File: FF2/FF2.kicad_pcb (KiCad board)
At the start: 2 copper layers, 154.8 x 140 mm, 76 parts, among them J1 AVR-ISP-6, SW1 RESET, SW2 BOOT, U1 ATmega328P-AU, Y1 16MHz

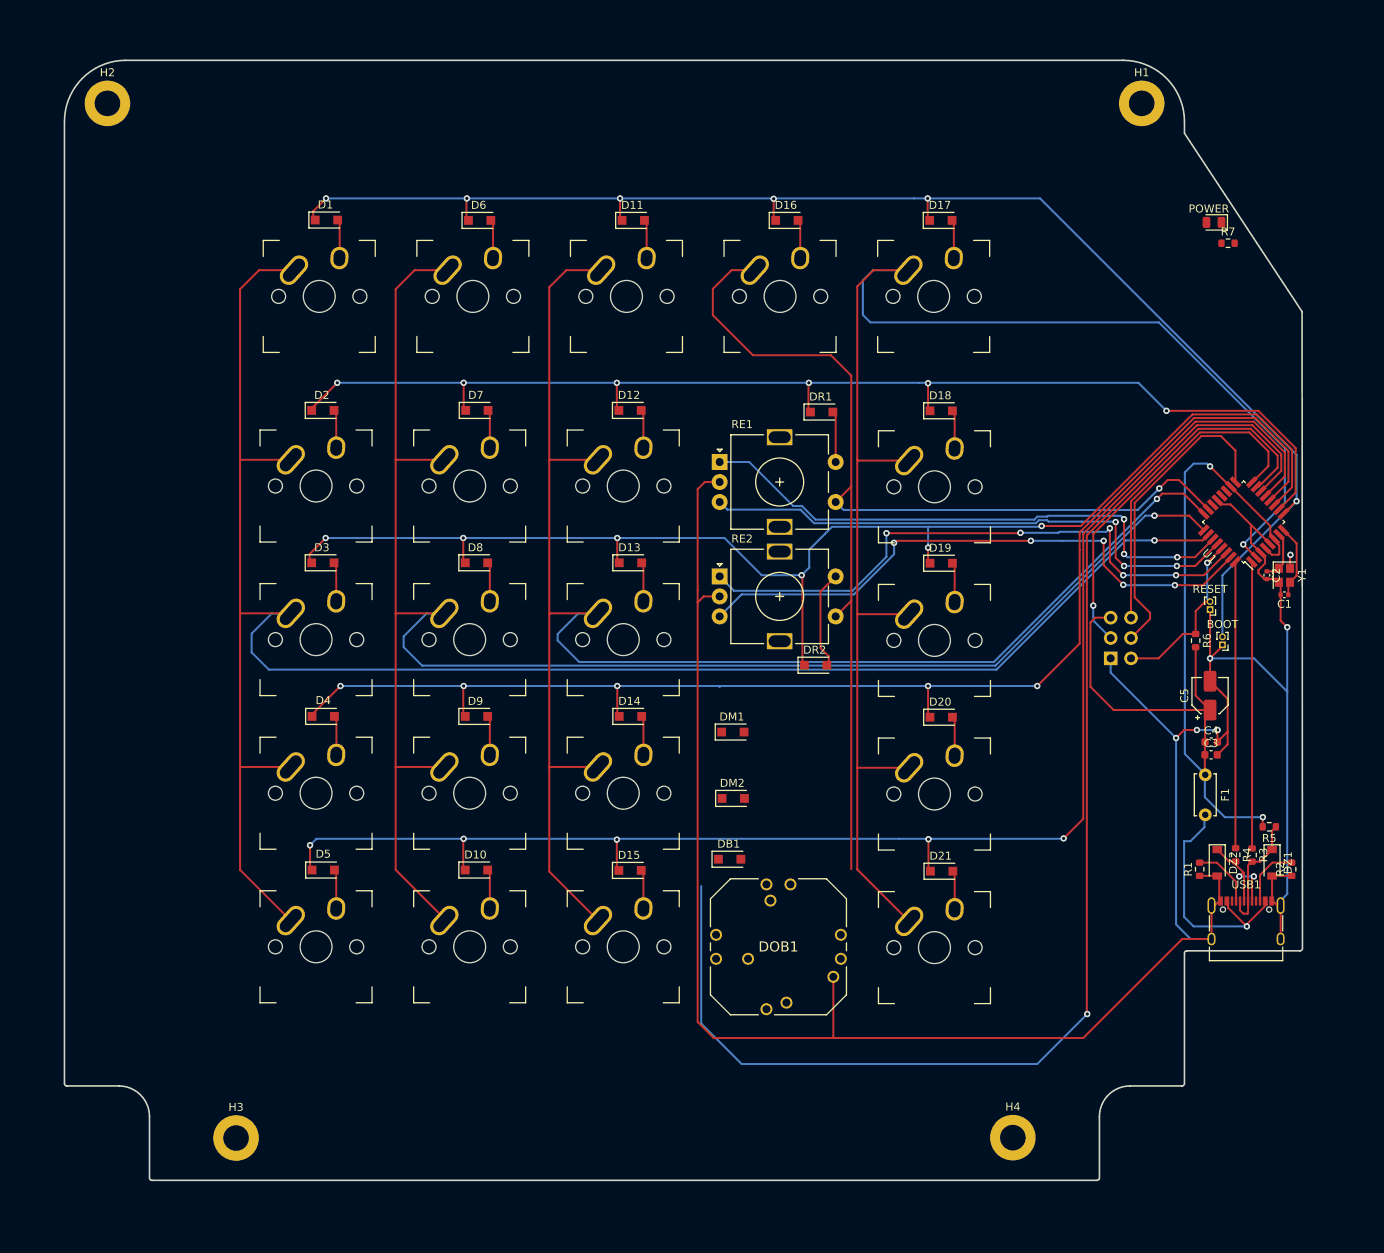
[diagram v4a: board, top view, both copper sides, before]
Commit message: updated silk values to be printed
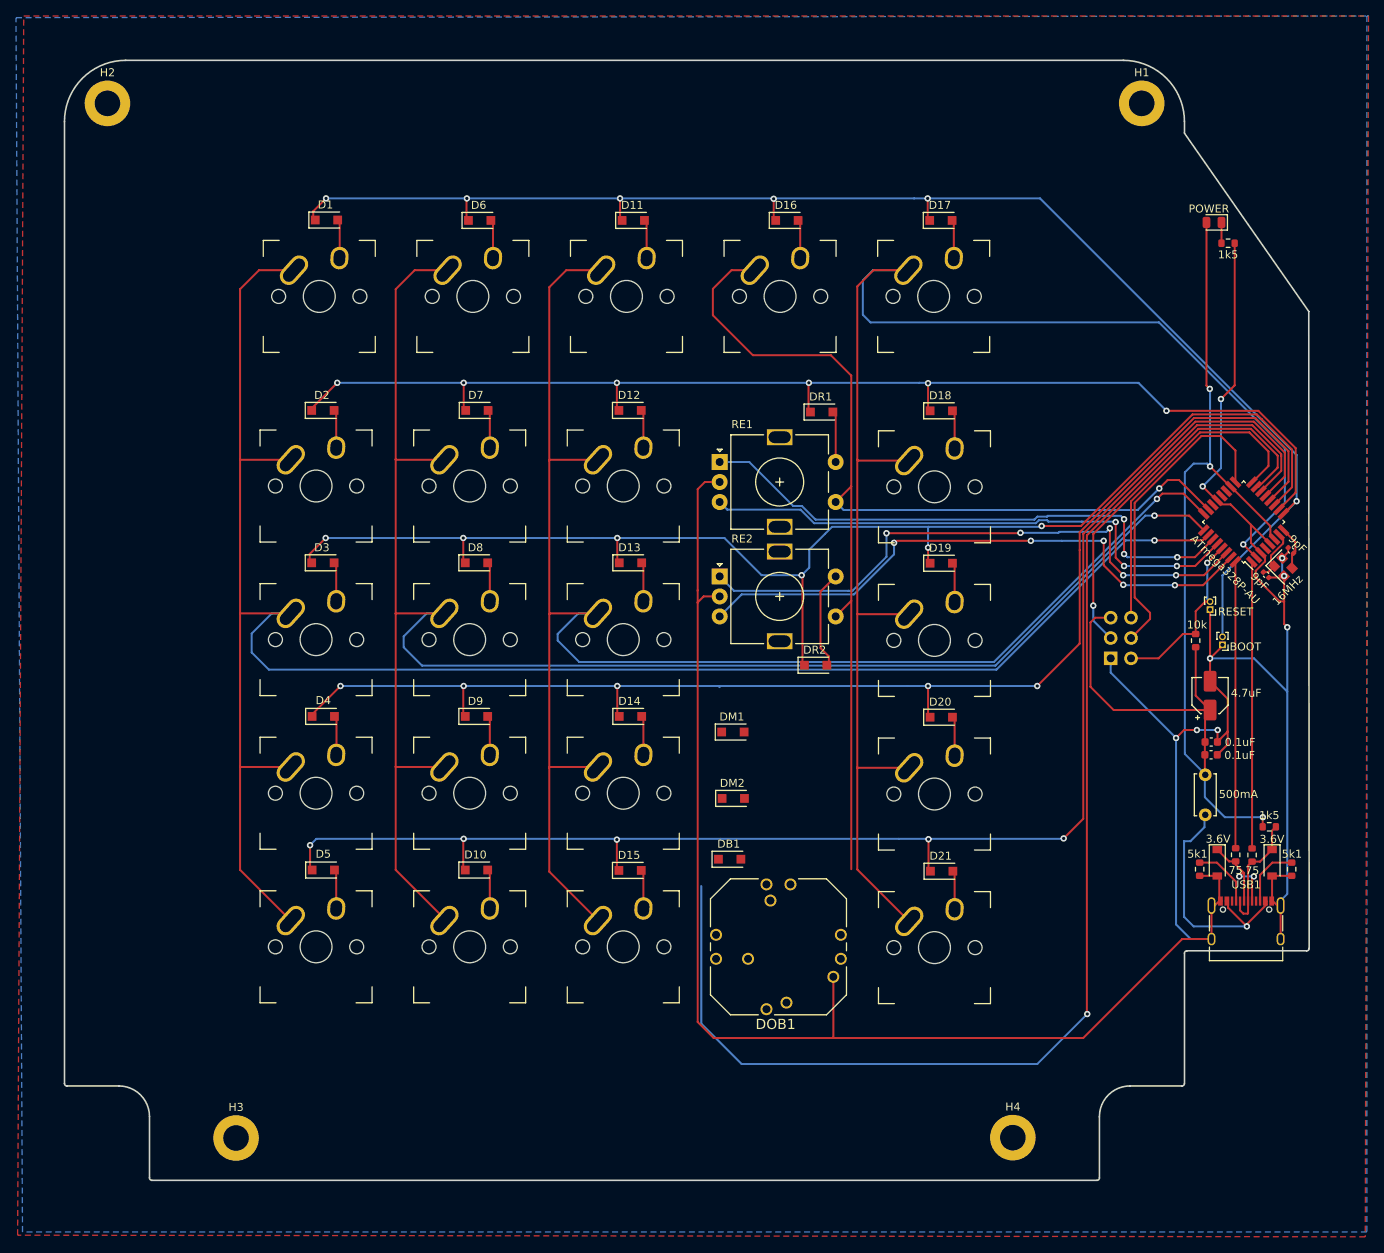
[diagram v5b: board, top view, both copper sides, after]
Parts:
- moved C1 5.61 mm to (235.1, 82.5), turned to 135 degrees
- moved Y1 1.03 mm to (234.1, 84.6), turned to 315 degrees
- moved C2 0.11 mm to (232.0, 85.6), turned to 315 degrees
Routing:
- net GND: track 319.3 -> 361.1 mm, vias 6 -> 9
- net +5V: track 115.4 -> 142.1 mm, vias 2 -> 3
- net CRYSTAL2: track 9.19 -> 5.51 mm
- net Net-(LED1-Pad1): track 0.00 -> 2.60 mm
- added copper zone on B.Cu, net GND
- added copper zone on F.Cu, net GND
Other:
- board size 154.8 x 140 mm -> 155.6 x 140 mm

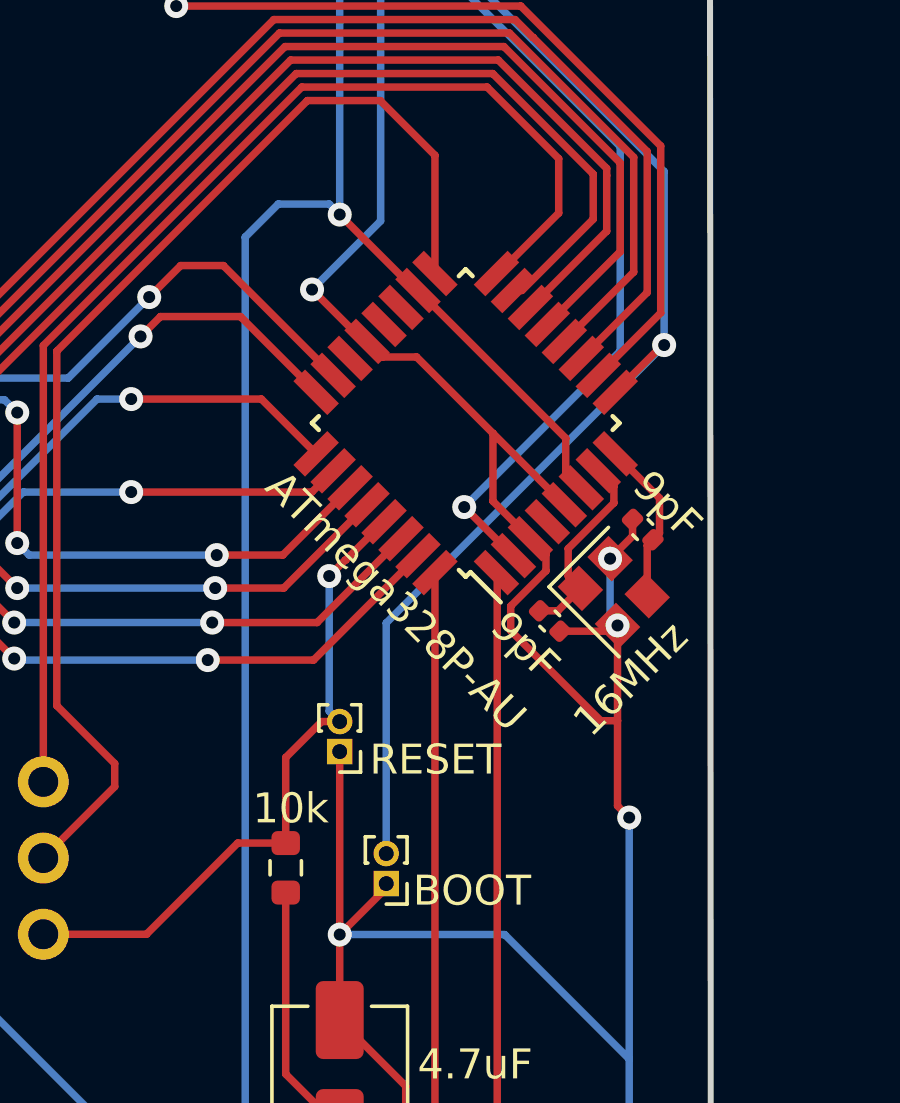
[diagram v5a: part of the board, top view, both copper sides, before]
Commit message: updated footprint for boot and reset headers
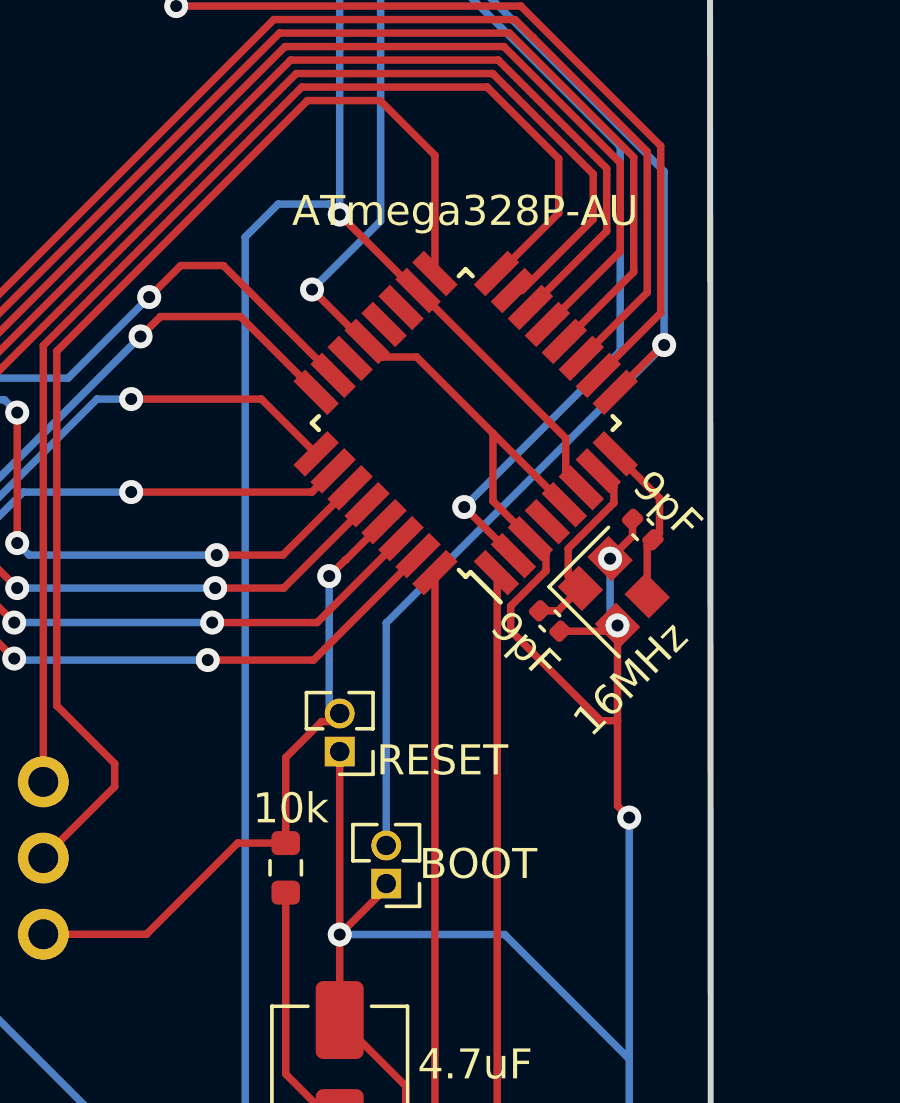
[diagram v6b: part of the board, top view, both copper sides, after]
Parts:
- SW1, SW2: footprint Connector_PinHeader_1.00mm:PinHeader_1x02_P1.00mm_Vertical -> Connector_PinHeader_1.27mm:PinHeader_1x02_P1.27mm_Vertical
